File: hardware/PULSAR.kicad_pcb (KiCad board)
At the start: 4 copper layers, 80 x 150 mm, 9 parts, among them J1 Conn_01x20, J2 Conn_01x04, J3 USB_C_Receptacle, U1 AP2112K-3.3, U2 SS49E, U3 CD74HC4067M, U4 ADS8688

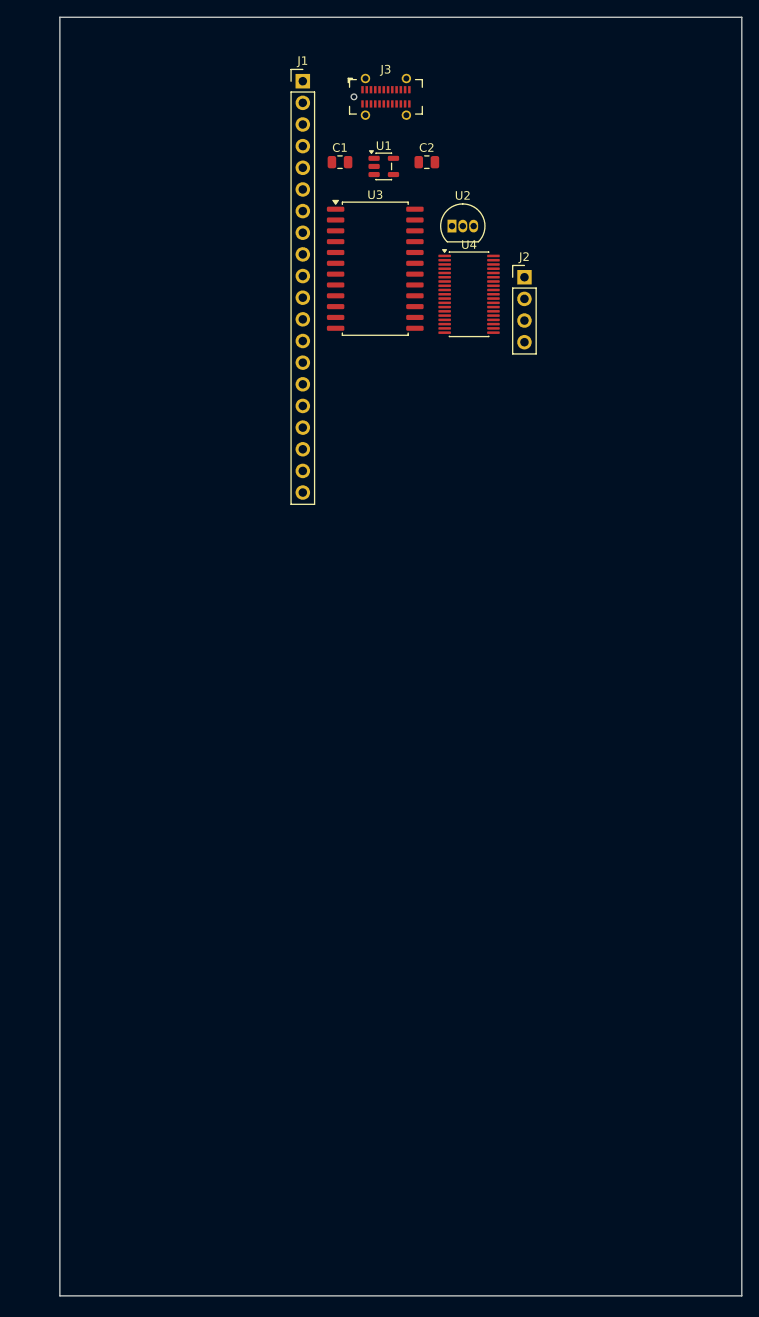
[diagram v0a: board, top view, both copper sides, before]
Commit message: feat: complete PCB routing and fix DRC errors
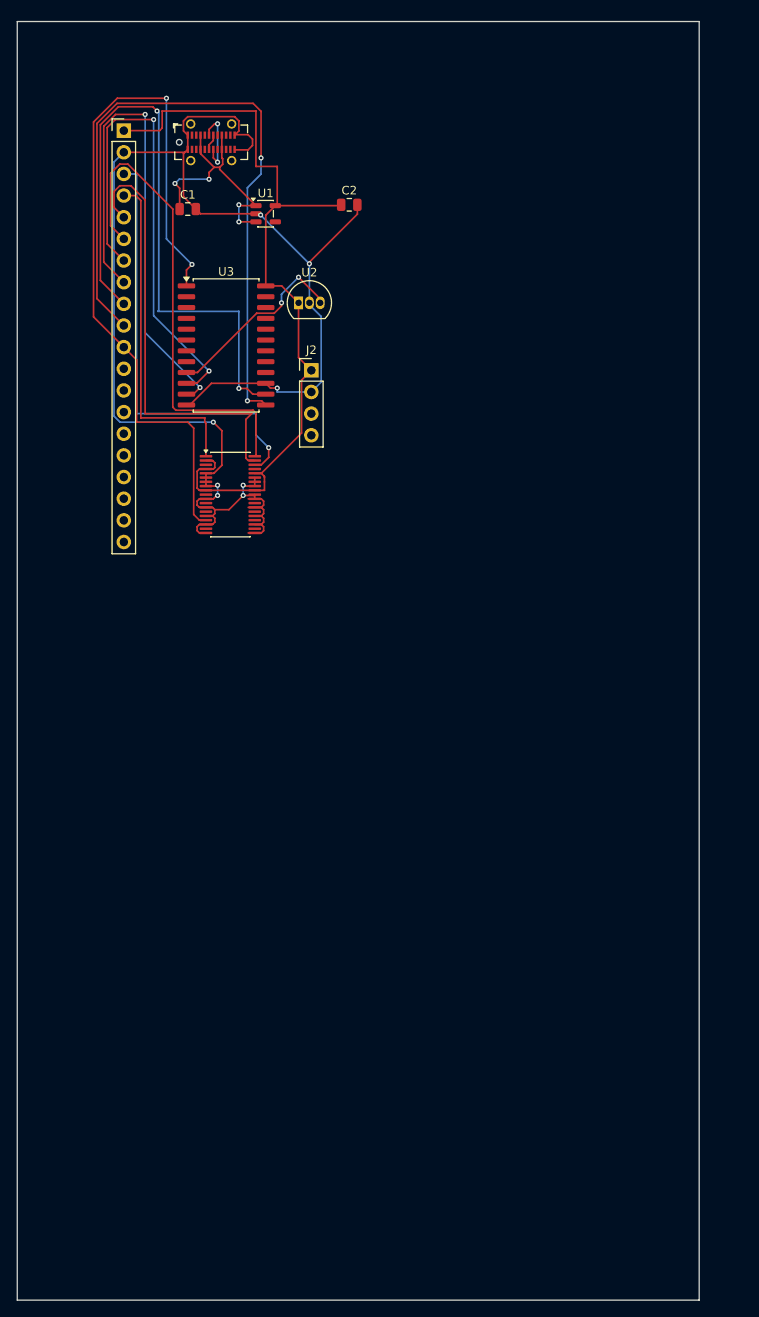
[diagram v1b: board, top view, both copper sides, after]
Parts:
- moved U4 36.6 mm to (123.5, 70.0)
- moved J2 27.3 mm to (133.0, 55.4)
- moved J1 21.8 mm to (111.0, 27.3)
- moved J3 21.2 mm to (121.2, 28.7)
- moved U2 20.1 mm to (131.5, 47.5)
- moved U3 19.7 mm to (123.0, 52.5)
- moved C1 18.7 mm to (118.5, 36.5)
- moved U1 14.9 mm to (127.6, 37.0)
- moved C2 10.4 mm to (137.4, 36.0)
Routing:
- net GND: track 0.00 -> 178.2 mm, vias 0 -> 8
- net +3.3V: track 0.00 -> 93.6 mm
- net /MUX_OUT: track 0.00 -> 89.4 mm, vias 0 -> 2
- net /MUX_S3: track 0.00 -> 82.6 mm, vias 0 -> 2
- net /MUX_S2: track 0.00 -> 75.5 mm, vias 0 -> 2
- net /MUX_S1: track 0.00 -> 61.3 mm, vias 0 -> 2
- net /MUX_S0: track 0.00 -> 57.7 mm, vias 0 -> 2
- net /SPI_CS1: track 0.00 -> 56.7 mm
- net /SPI_SCLK: track 0.00 -> 52.3 mm
- net /SPI_SDO: track 0.00 -> 51.3 mm, vias 0 -> 1
- net /SPI_SDI: track 0.00 -> 39.8 mm
- net +5V: track 0.00 -> 30.4 mm, vias 0 -> 4
- net /HALL_OUT_1: track 0.00 -> 22.6 mm, vias 0 -> 2
- net /USB_DP: track 0.00 -> 8.15 mm, vias 0 -> 2
- net /USB_DN: track 0.00 -> 1.88 mm
